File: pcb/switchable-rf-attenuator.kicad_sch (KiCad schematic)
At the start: 20 parts, among them J1 USB_B_Mini, J2 Conn_Coaxial, J3 Conn_Coaxial, SW1 SW_SPDT, U1 AS179-92LF, U2 AS179-92LF

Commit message: add assets
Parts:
- removed U1, U2: AS179-92LF, Package_TO_SOT_SMD:SOT-363_SC-70-6, symbol RF_Switch:AS179-92LF
- added H1, H2, H3, H4: MountingHole_Pad, MountingHole:MountingHole_2.2mm_M2_Pad_Via, symbol Mechanical:MountingHole_Pad
- added U1, U2: AS183-73LF, Package_TO_SOT_SMD:SOT-363_SC-70-6, symbol Kevin_Lutzer_Lbr:AS183-73LF
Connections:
- net GND: now also U1.6 (V2), U2.4 (V1)
- net GNDA: now also H1.1, H2.1, H3.1, H4.1, U1.2 (GND), U2.2 (GND)
- net IN: now also U1.5 (J1)
- net OUT: now also U2.5 (J1)
- net PASS_THRU_IN: now also U1.1 (J3)
- net PASS_THRU_OUT: now also U2.3 (J2)
- net T_IN: now also U1.3 (J2)
- net T_OUT: now also U2.1 (J3)
- net V_CTL: now also U1.4 (V1), U2.6 (V2)
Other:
- note added: "F(3db) = 6Mhz for a 0.33p C2, C1 6db attenuation"
- note added: "Mounting Holes"
- note removed: "F(3db) = 6Mhz for a 0.33p C2, C1"
- company: (none) -> Kevin Lutzer
- title: (none) -> RF Attenutation with Switchable Pass Thru

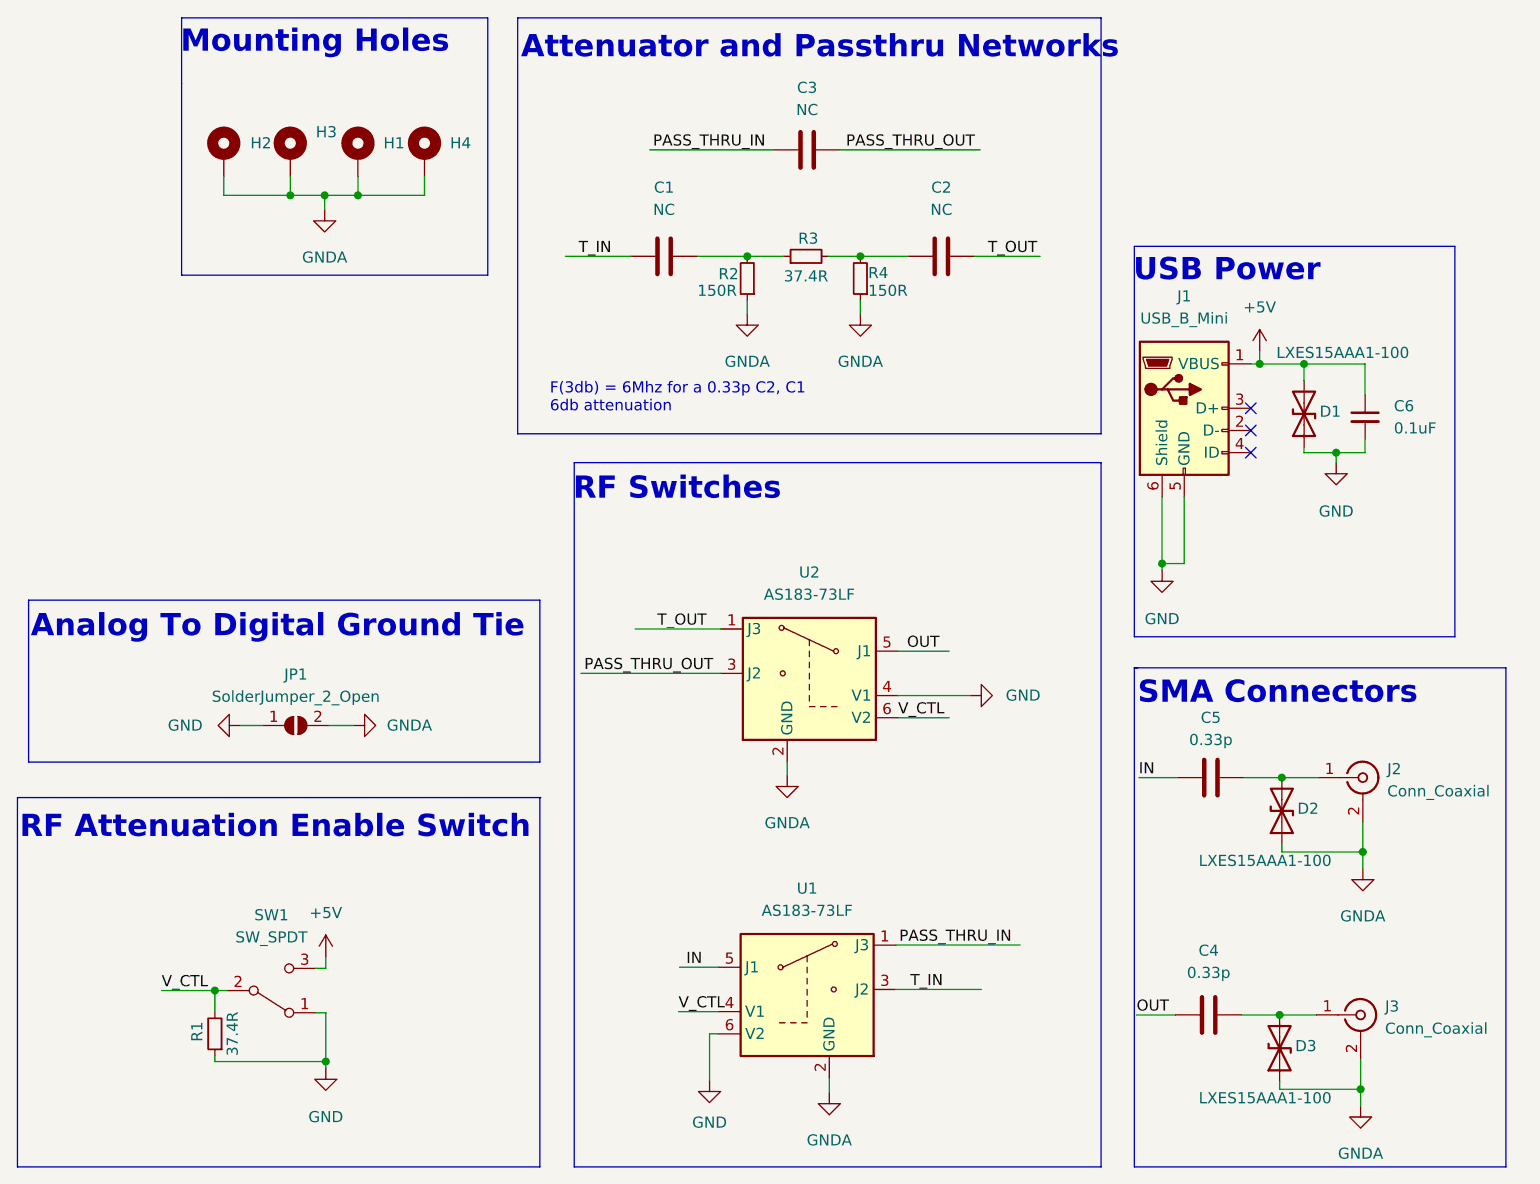
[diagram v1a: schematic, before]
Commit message: add bom and add a LPF for the DC signals
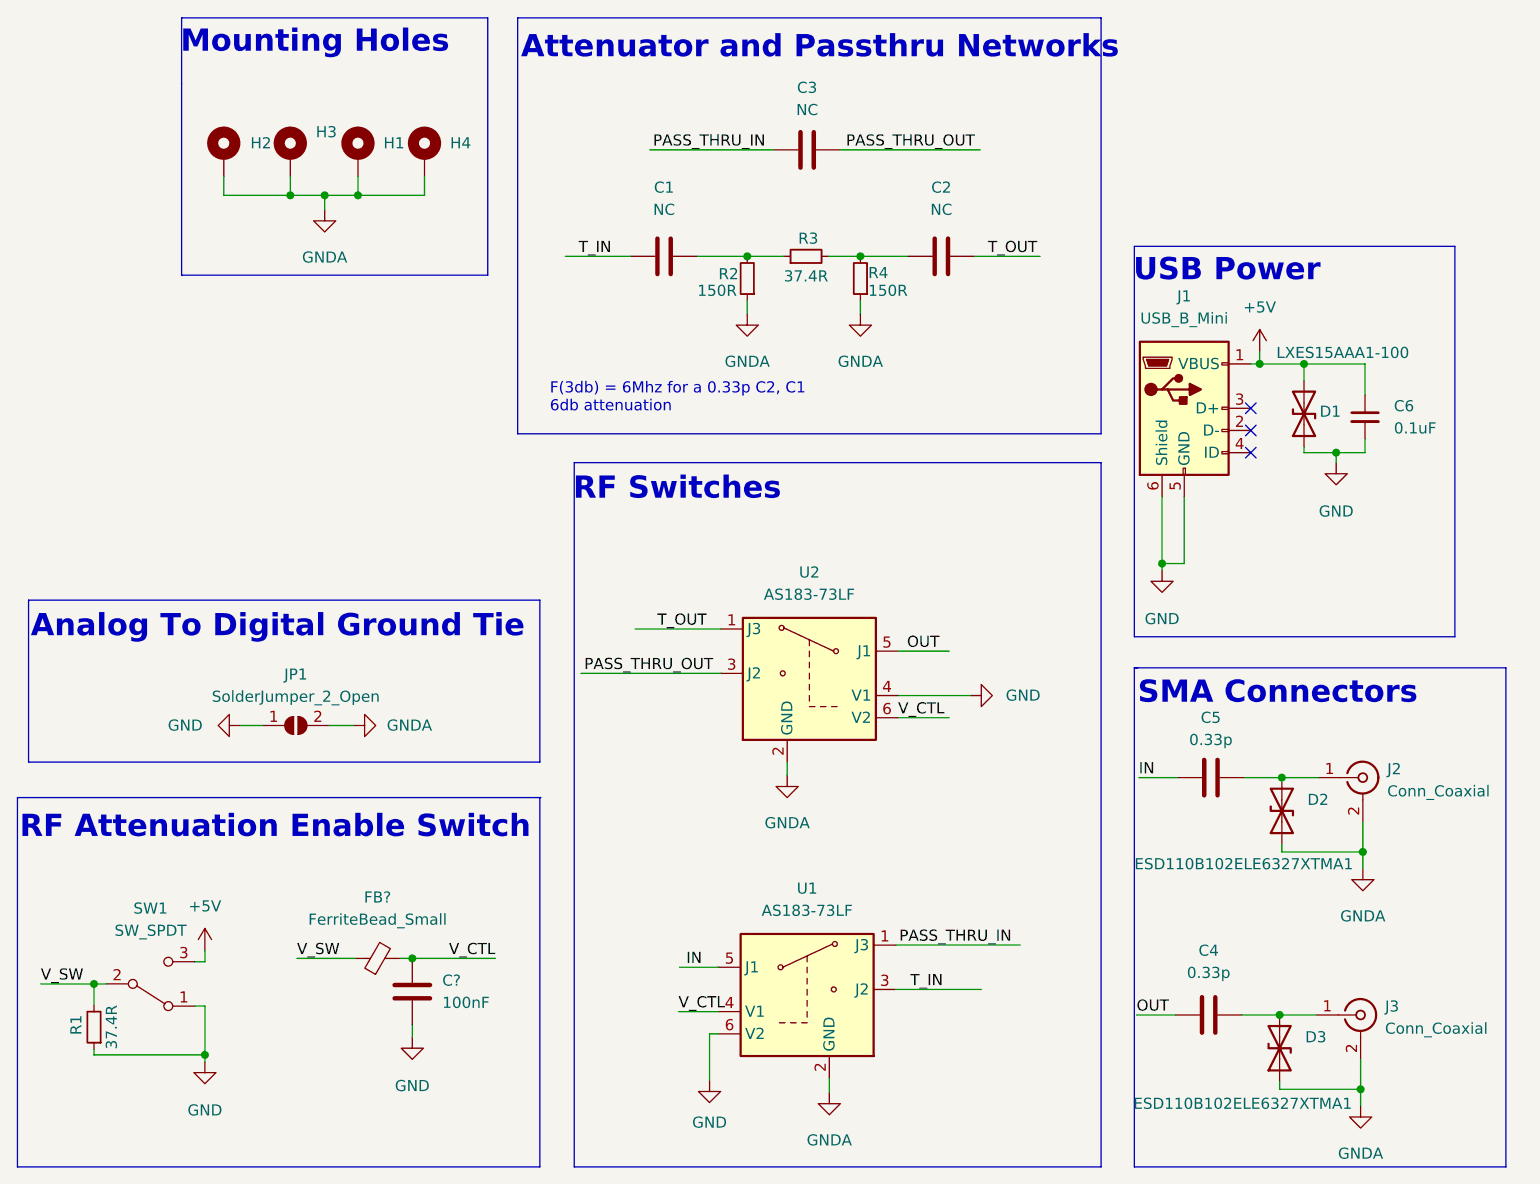
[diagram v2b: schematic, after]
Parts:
- removed D2, D3: LXES15AAA1-100, Diode_SMD:D_0402_1005Metric, symbol Device:D_TVS
- added C?: 100nF, Capacitor_SMD:C_0603_1608Metric, symbol Device:C
- added D2, D3: ESD110B102ELE6327XTMA1, Diode_SMD:D_0402_1005Metric, symbol Kevin_Lutzer_Lbr:ESD110B102ELE6327XTMA1
- added FB?: FerriteBead_Small, Inductor_SMD:L_0603_1608Metric, symbol Device:FerriteBead_Small
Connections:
- net GND: now also C?.2
- net GNDA: now also D2.1 (A1), D3.1 (A1)
- net V_CTL: now also C?.1, FB?.2; no longer R1.2, SW1.2 (B)
- net at C5.2, J2.1 (In): now also D2.2 (A2)
- net at C4.2, J3.1 (In): now also D3.2 (A2)
- new net V_SW: FB?.1, R1.2, SW1.2 (B)
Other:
- moved on the sheet: R1, SW1

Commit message: cleanup FB1
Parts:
- gave numbers to parts that had none: 2
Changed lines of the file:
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@@
   (symbol (lib_id "Device:FerriteBead_Small") (at 99.314 133.985 90) (unit 1)
     (in_bom yes) (on_board yes) (fields_autoplaced)
-    (property "Reference" "FB?" (id 0) (at 99.2759 127 90))
+    (property "Reference" "FB1" (id 0) (at 99.2759 127 90))
     (property "Value" "FerriteBead_Small" (id 1) (at 99.2759 129.54 90))
     (property "Footprint" "Inductor_SMD:L_0603_1608Metric" (id 2) (at 99.314 135.763 90)
@@
   (symbol (lib_id "Device:C") (at 103.251 137.795 0) (unit 1)
     (in_bom yes) (on_board yes) (fields_autoplaced)
-    (property "Reference" "C?" (id 0) (at 106.68 136.5249 0)
+    (property "Reference" "C7" (id 0) (at 106.68 136.5249 0)
       (effects (font (size 1.27 1.27)) (justify left))
     )
@@
   (symbol (lib_id "power:GND") (at 103.251 143.002 0) (unit 1)
     (in_bom yes) (on_board yes) (fields_autoplaced)
-    (property "Reference" "#PWR?" (id 0) (at 103.251 149.352 0)
+    (property "Reference" "#PWR0117" (id 0) (at 103.251 149.352 0)
       (effects (font (size 1.27 1.27)) hide)
     )
@@
     )
     (path "/eedde049-ed44-4c5e-837b-9065af28a6f6"
-      (reference "#PWR?") (unit 1) (value "GND") (footprint "")
+      (reference "#PWR0117") (unit 1) (value "GND") (footprint "")
     )
     (path "/0f0002d8-f051-4915-b9d0-55866a37abce"
@@
     )
     (path "/b95ccc36-bd6e-4624-9628-3cc7faa4d6c3"
-      (reference "C?") (unit 1) (value "100nF") (footprint "Capacitor_SMD:C_0603_1608Metric")
+      (reference "C7") (unit 1) (value "100nF") (footprint "Capacitor_SMD:C_0603_1608Metric")
     )
     (path "/a9264ea1-c27c-45dc-99bc-45e827b8b425"
@@
     )
     (path "/4e53cca6-8de7-45d2-93a3-52bc7a0091e1"
-      (reference "FB?") (unit 1) (value "FerriteBead_Small") (footprint "Inductor_SMD:L_0603_1608Metric")
+      (reference "FB1") (unit 1) (value "FerriteBead_Small") (footprint "Inductor_SMD:L_0603_1608Metric")
     )
     (path "/ec842cc0-ee82-4195-b926-1b7209911110"
